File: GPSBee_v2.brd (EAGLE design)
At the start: 24.5 x 27.6 mm, 60 parts, among them J1 MICRO-USB-5P-340015001, U1 UBLOX-LEA-6T, U2 TPS73633, U3 TPS73633, X1 SERIAL, X2 ANT, X3 FOUT, X4 ANT, X5 FOUT, X6 1PPS, X7 PC, X8 1PPS, X9 22-23-2021

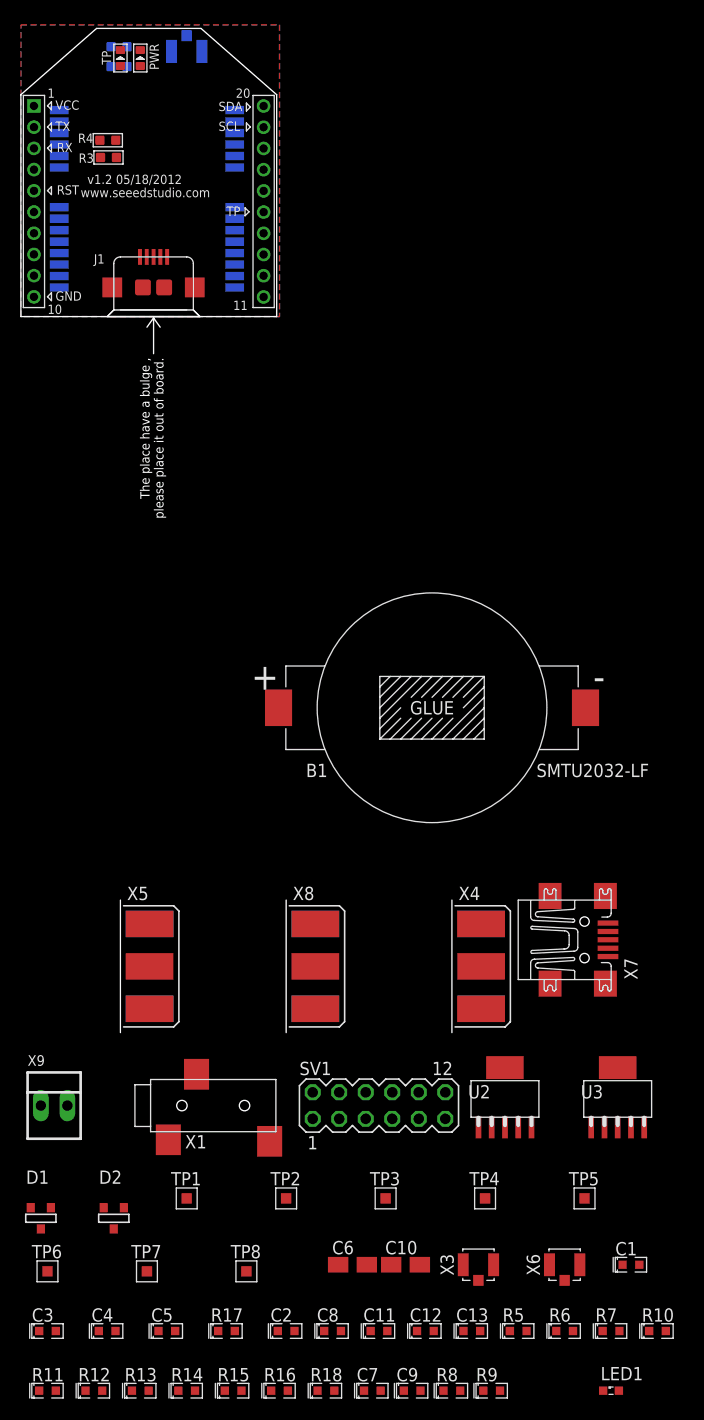
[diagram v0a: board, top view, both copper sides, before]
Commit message: Pulled in design from osmo-lea-6T board
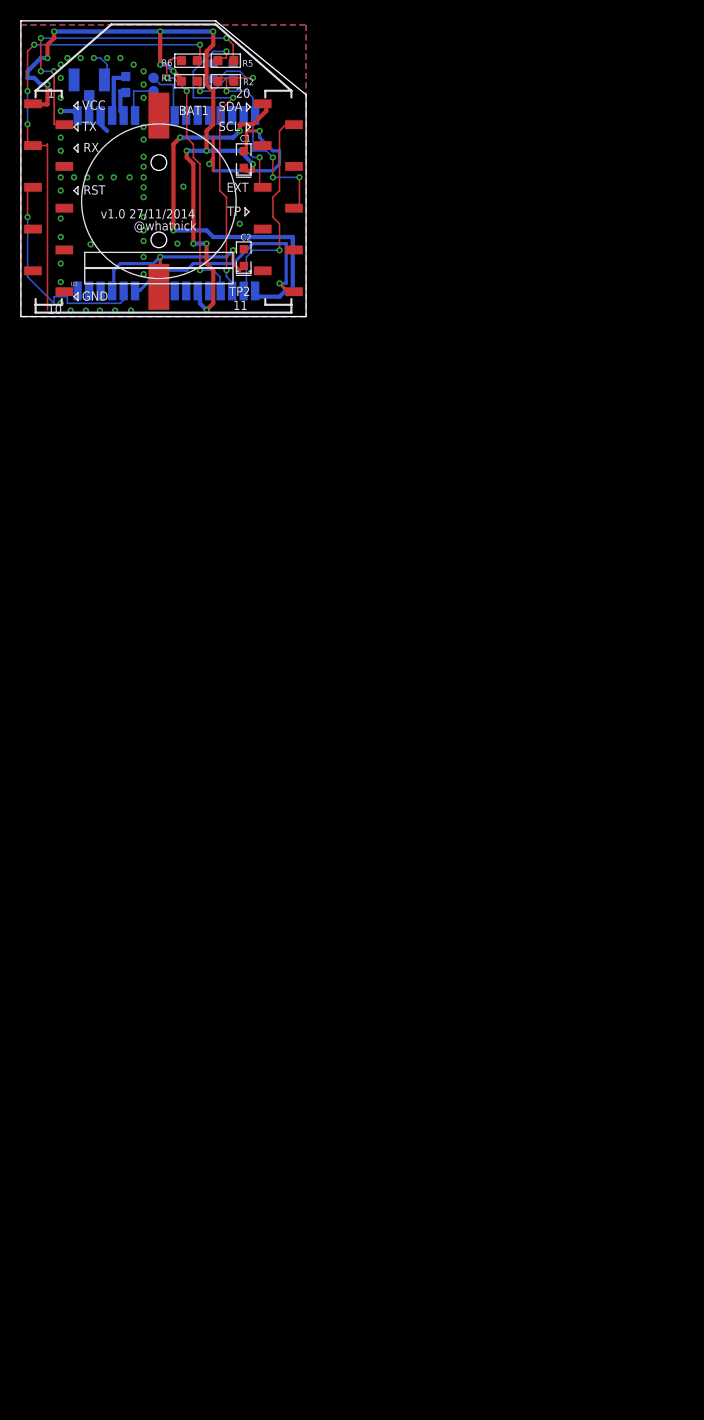
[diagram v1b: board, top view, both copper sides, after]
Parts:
- removed B1: SMTU2032-LF, we_misc:SMTU2032
- removed C10, C6: 10u, rcl:A/3216-18R
- removed C11, C13, C7, C9: 1u, we_passive:0603
- removed C12, C8: 10n, we_passive:0603
- removed C3, C4, C5: 100n, we_passive:0603
- removed D1, D2: BAT54, we_passive:SOT23
- removed J1: MICRO-USB-5P-340015001, Connector:B-SMD-5P
- removed LED1: (no value), led:SML0603
- removed R10, R11, R15, R9: 0R, we_passive:0603
- removed R12: 1k, we_passive:0603
- removed R13, R14, R18: DNP, we_passive:0603
- removed R16, R8: 1M, we_passive:0603
- removed R17: 220R, we_passive:0603
- removed R4: 330, Discrete:0603
- removed R7: 10R, we_passive:0603
- removed SV1: (no value), con-lstb-tnt:MA06-2
- removed TP3, TP4, TP5, TP6, TP7, TP8: TESTPAD, we_conn:TP_1X1
- removed U2: TPS73633, laforge:SOT223-6
- removed X1: SERIAL, laforge:JACK2.5_SJ-2523
- removed X3: FOUT, we_conn:HRS_UFL
- removed X4: ANT, we_conn:SMA-F-S-EDGE
- removed X5: FOUT, we_conn:SMA-F-S-EDGE
- removed X6: 1PPS, we_conn:HRS_UFL
- removed X7: PC, con-hirose:UX60-MB-5ST
- removed X8: 1PPS, we_conn:SMA-F-S-EDGE
- removed X9: 22-23-2021, con-molex:22-23-2021
- removed XBEE: XBEEEXT, EXT_moudle:XBEE_PLUG
- added BAT1: CR1220, Connector:PLASTIC-CR1220-L15.06XW13.0XH4.1MM
- R3: value 330 -> 10R
- R5, R6: value 22R -> 330; device we_passive:0603 -> Discrete:0603
- TP1, TP2: value TESTPAD -> TPTP10R; device we_conn:TP_1X1 -> testpad:TP10R
- U3: value TPS73633 -> XBEE-1B3; device laforge:SOT223-6 -> SparkFun-RF:XBEE-SMD
- moved R6 126.9 mm to (16.1, 24.5)
- moved R5 124.8 mm to (19.6, 24.5)
- moved C1 112.2 mm to (21.3, 15.0), turned to 90 degrees
- moved TP2 108.1 mm to (12.7, 22.9), flipped to the bottom
- moved TP1 106.1 mm to (12.7, 21.6), flipped to the bottom
- moved C2 102.9 mm to (21.3, 5.65), turned to 90 degrees
- moved U3 87.0 mm to (13.7, 0.38)
- moved R2 10.3 mm to (19.6, 22.5), flipped to the top
- moved X2 9.73 mm to (6.54, 22.7), turned to 0 degrees
- moved PWR 8.98 mm to (20.3, 23.5), flipped to the bottom
- moved TP 8.98 mm to (18.4, 23.5), flipped to the bottom
- moved R1 7.50 mm to (16.1, 22.5), flipped to the top
- moved R3 7.18 mm to (10.0, 22.2), flipped to the bottom, turned to 90 degrees
- moved U1 1.81 mm to (13.8, 10.9), turned to 270 degrees
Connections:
- removed net 1PPS_EXT: R15.2, SV1.10
- removed net EX: XBEE.5
- removed net FOUT: R11.1, U1.9, X3.SIG, X5.C
- removed net FOUT_EXT: R11.2, SV1.9
- removed net N$10: J1.2
- removed net N$11: J1.3
- removed net N$12: J1.5, J1.E1, J1.E2, J1.P1, J1.P2
- removed net N$13: R6.1, X7.3
- removed net N$14: R5.1, X7.2
- removed net N$17: TP3.TP, U1.21
- removed net N$18: TP5.TP, U1.22
- removed net N$19: TP6.TP, U1.23
- removed net N$20: R10.1, X2.SIG
- removed net N$22: TP1.TP, U1.12
- removed net N$23: TP4.TP, U1.8
- removed net N$24: TP7.TP, U1.5
- removed net N$25: R9.1, X4.C
- removed net N$27: TP2.TP, U1.20
- removed net N$28: C10.+, C11.1, U3.1, U3.5, X9.1
- removed net N$29: C12.1, U3.4
- removed net N$30: C13.1, D2.1, R13.1, U3.2
- removed net N$31: R12.2, R13.2, U2.5
- removed net N$32: C8.1, U2.4
- removed net N$33: C4.1, R8.2, X7.M1, X7.M4
- removed net N$34: C5.1, R16.2, X7.M2, X7.M3
- removed net N$35: LED1.C, R17.2
- removed net N$36: R18.1, TP8.TP
- removed net N$7: R6.2, U1.26
- removed net N$8: XBEE.16
- removed net N$9: J1.1
- removed net SERIAL_RXD: SV1.5, U1.4, X1.2
- removed net SERIAL_TXD: SV1.3, U1.3, X1.3
- removed net TP: R2.1, XBEE.15
- removed net VBUS: C7.1, R12.1, U2.1, X7.1
- removed net VUSB: C3.1, C9.1, D1.1, R14.2, U1.24, U2.2
- new net TP2: U1.9, U3.11
- new net VCC_OUT: U1.8
- new net VDDUSB: U1.24
- net !RESET: now also U3.5; no longer SV1.2
- net 1PPS: now also R2.1, U3.15; no longer R15.1, X6.SIG, X8.C
- net 3V3: now also U3.1; no longer C6.+, D1.3, D2.3, LED1.A, SV1.12, XBEE.1
- net GND: now also BAT1.-, U3.10; no longer B1.-, C10.-, C11.2, C12.2, C13.2, C3.2, C4.2, C5.2, C6.-, C7.2, C8.2, C9.2, R14.1, R16.1, R17.1, R8.1, SV1.1, SV1.11, SV1.7, U2.3, U2.6, U3.3, U3.6, X1.1, X3.GND@1, X3.GND@2, X4.BG1, X4.BG2, X4.TG1, X4.TG2, X5.BG1, X5.BG2, X5.TG1, X5.TG2, X6.GND@1, X6.GND@2, X7.5, X8.BG1, X8.BG2, X8.TG1, X8.TG2, X9.2, XBEE.10
- net INT: now also U3.16; no longer SV1.8
- net N$15: now also R3.2; no longer R7.2
- net N$16: now also R3.1; no longer R18.2, R7.1
- net N$2: now also R6.2, U3.3; no longer X7.4
- net N$21: now also BAT1.+; no longer B1.+
- net N$26: now also X2.SIG; no longer R10.2, R9.2
- net N$3: now also TP1.TP, U1.20; no longer R5.2, U1.25
- net N$4: now also R5.2, U3.2; no longer R3.2, XBEE.3
- net N$6: now also TP2.TP, U1.21; no longer R4.2, XBEE.2
- net RX_GPS: now also R6.1, U1.4; no longer R3.1
- net SCL: now also U3.19; no longer SV1.6, XBEE.19
- net SDA: now also U3.20; no longer SV1.4, XBEE.20
- net TX_GPS: now also R5.1, U1.3; no longer R4.1
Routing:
- net 3V3: track 0.00 -> 72.7 mm, vias 0 -> 13
- net N$2: track 0.00 -> 45.1 mm, vias 0 -> 4
- net SDA: track 0.00 -> 41.3 mm, vias 0 -> 3
- net TX_GPS: track 0.00 -> 31.5 mm, vias 0 -> 3
- net N$4: track 0.00 -> 30.7 mm, vias 0 -> 4
- net RX_GPS: track 0.00 -> 26.7 mm, vias 0 -> 3
- net GND: track 0.00 -> 25.0 mm, vias 0 -> 50
- net TP2: track 0.00 -> 22.8 mm, vias 0 -> 1
- net !RESET: track 0.00 -> 21.6 mm, vias 0 -> 1
- net N$21: track 0.00 -> 20.6 mm, vias 0 -> 2
- net SCL: track 0.00 -> 20.5 mm, vias 0 -> 1
- net 1PPS: track 0.00 -> 20.1 mm, vias 0 -> 4
- net INT: track 0.00 -> 8.01 mm, vias 0 -> 1
- net N$5: track 0.00 -> 6.69 mm, vias 0 -> 1
- net N$6: track 0.00 -> 5.15 mm
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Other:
- board size 24.5 x 27.6 mm -> 27.3 x 28.3 mm
- board text added: "@whatnick"
- board text added: "EXT"
- board text added: "TP2"
- board text added: "v1.0 27/11/2014"
- board text removed: "v1.2 05/18/2012"
- board text removed: "www.seeedstudio.com"

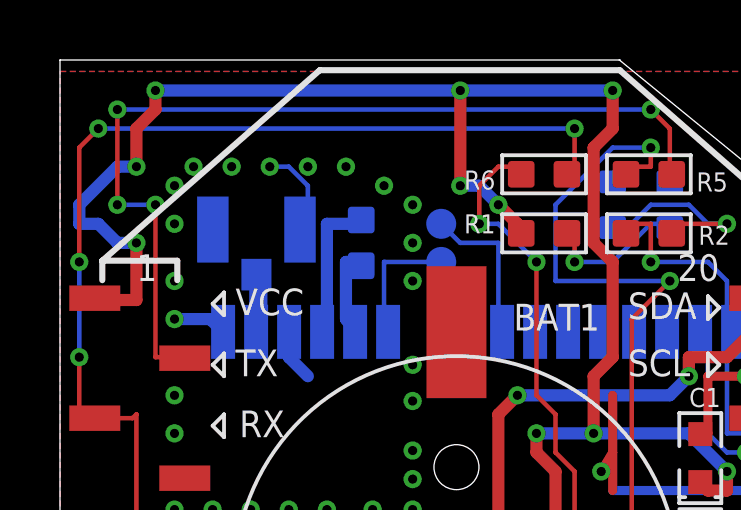
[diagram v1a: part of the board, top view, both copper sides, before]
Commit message: Widened power trace
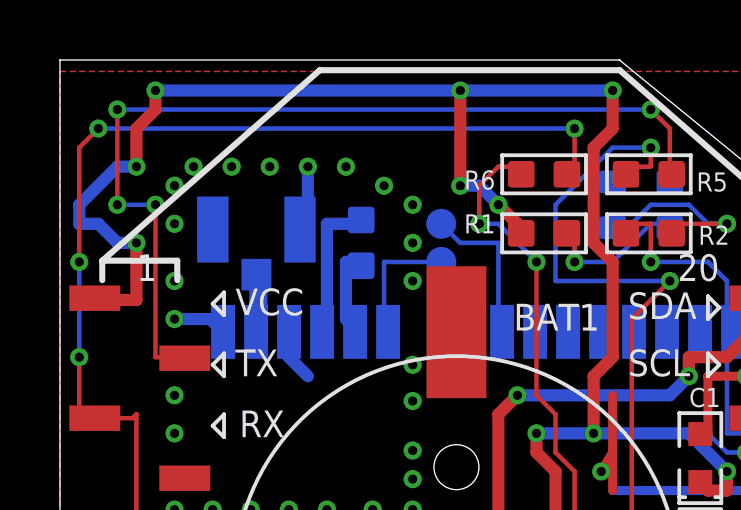
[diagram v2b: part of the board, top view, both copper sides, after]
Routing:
- net GND: track 25.0 -> 24.1 mm
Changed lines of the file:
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@@
 <layer number="17" name="Pads" color="2" fill="1" visible="yes" active="yes"/>
 <layer number="18" name="Vias" color="2" fill="1" visible="yes" active="yes"/>
-<layer number="19" name="Unrouted" color="6" fill="1" visible="no" active="yes"/>
+<layer number="19" name="Unrouted" color="6" fill="1" visible="yes" active="yes"/>
 <layer number="20" name="Dimension" color="5" fill="1" visible="yes" active="yes"/>
 <layer number="21" name="tPlace" color="7" fill="1" visible="yes" active="yes"/>
@@
 <via x="3.81" y="24.13" extent="1-16" drill="0.3048"/>
 <via x="20.955" y="8.89" extent="1-16" drill="0.3048"/>
-<wire x1="8.255" y1="22.86" x2="8.255" y2="24.13" width="0.1524" layer="16"/>
 <wire x1="8.255" y1="22.86" x2="7.993" y2="22.6695" width="0.1524" layer="16"/>
-<wire x1="7.62" y1="24.765" x2="8.255" y2="24.13" width="0.1524" layer="16"/>
-<wire x1="6.985" y1="24.765" x2="7.62" y2="24.765" width="0.1524" layer="16"/>
 <wire x1="3.81" y1="19.685" x2="5.003" y2="19.685" width="0.4064" layer="16"/>
 <wire x1="5.003" y1="19.685" x2="5.4295" y2="19.2585" width="0.4064" layer="16"/>
@@
 <via x="10.414" y="13.335" extent="1-16" drill="0.3048"/>
 <via x="11.7475" y="7.239" extent="1-16" drill="0.3048"/>
+<wire x1="8.255" y1="22.86" x2="8.255" y2="24.765" width="0.4064" layer="16"/>
 </signal>
 <signal name="RX_GPS">
